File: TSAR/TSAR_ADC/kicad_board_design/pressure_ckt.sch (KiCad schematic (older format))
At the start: 20 parts, among them U10 MCP3424T-E/ST

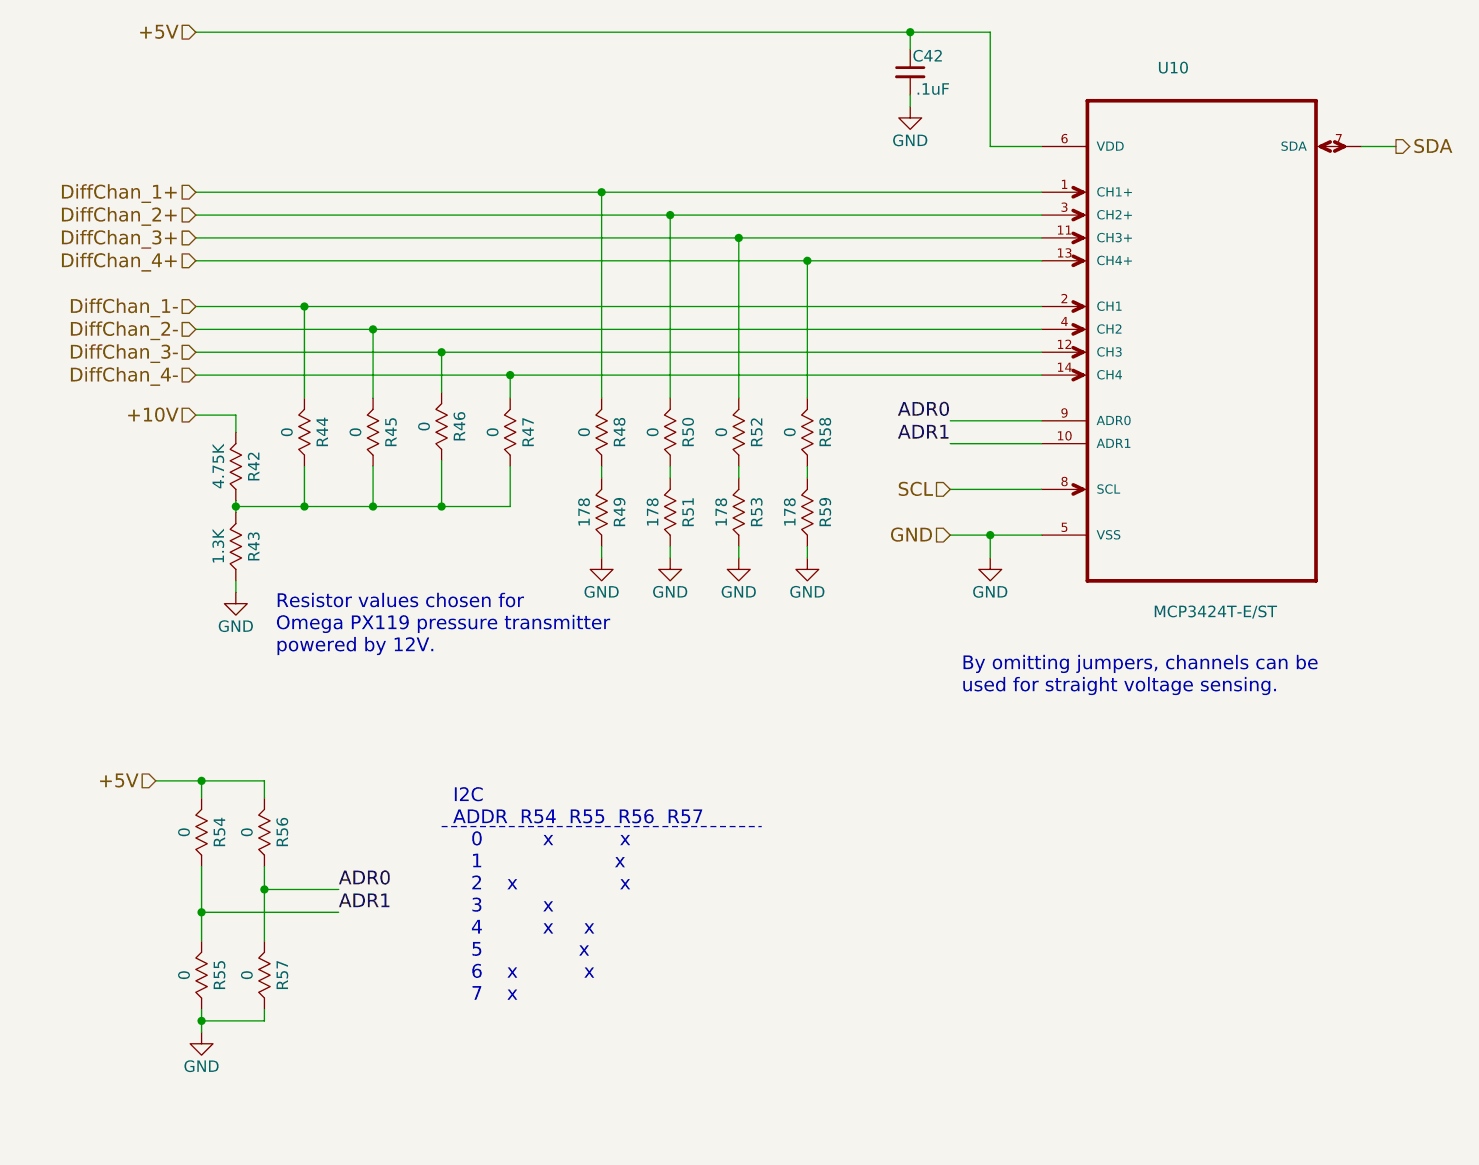
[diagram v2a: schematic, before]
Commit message: Incorporate review comments.  Improve U1 routing, general schematic comments.
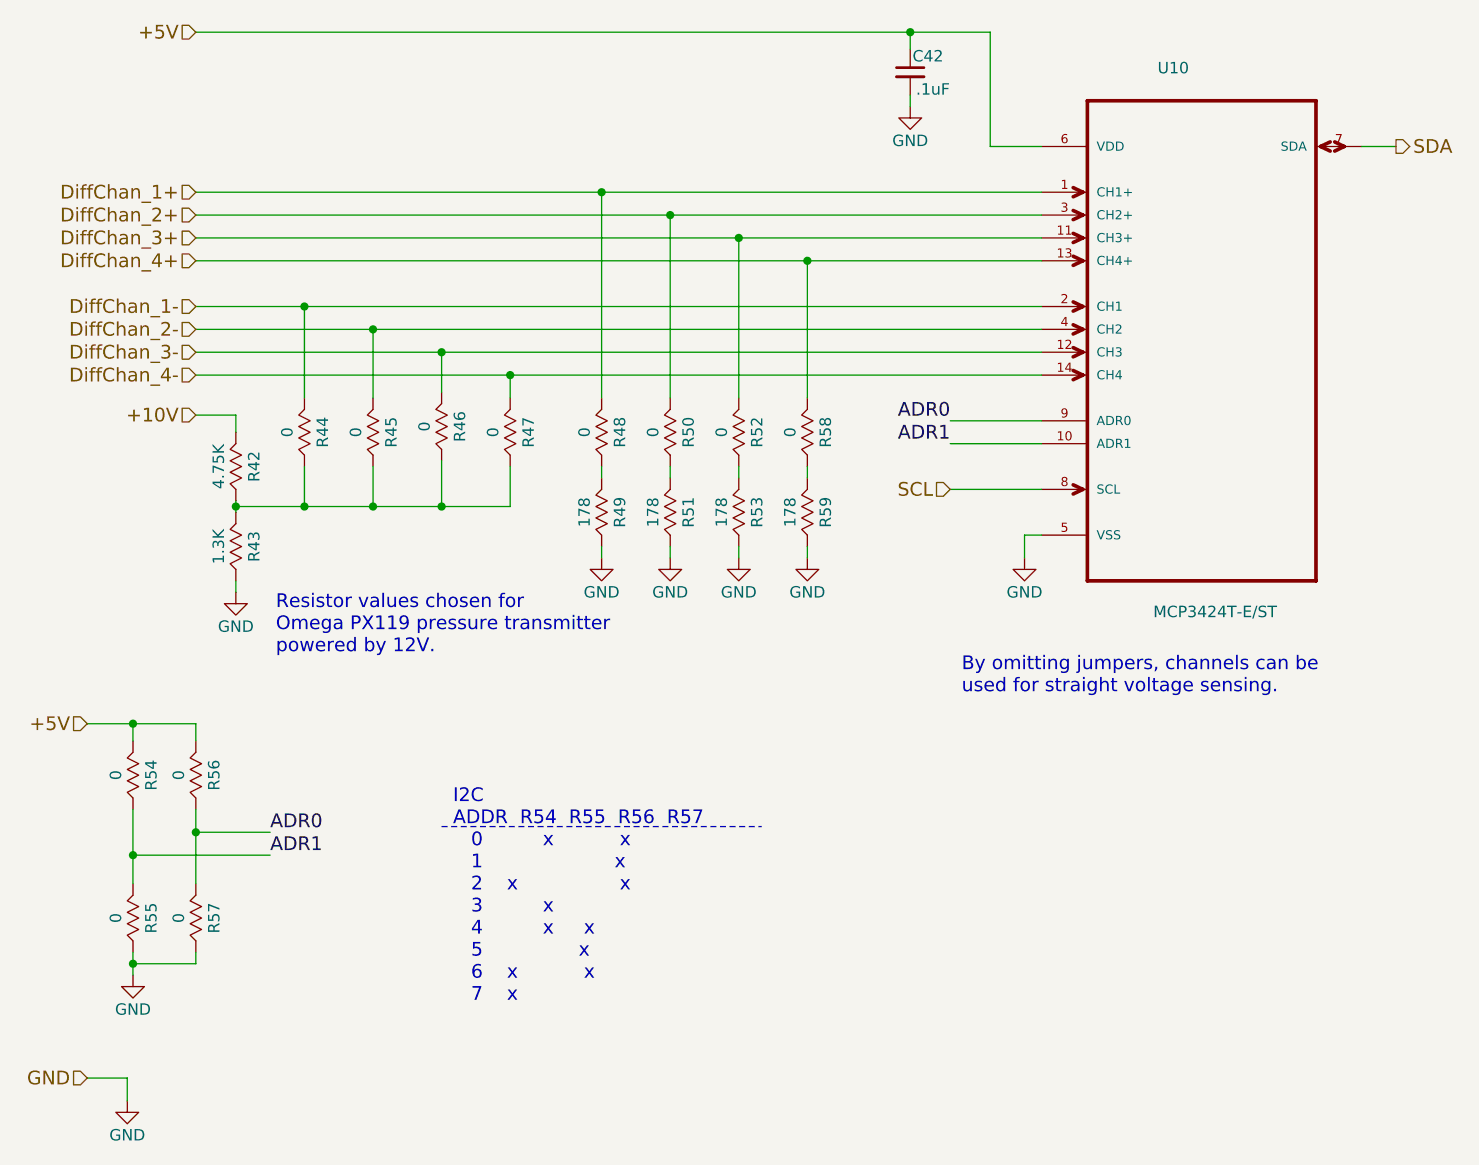
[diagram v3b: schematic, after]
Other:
- moved on the sheet: R54, R55, R56, R57
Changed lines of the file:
@@
 L GND #PWR056
 U 1 1 5B5D17AF
-P 6800 4825
-F 0 "#PWR056" H 6800 4575 50  0001 C CNN
-F 1 "GND" H 6800 4675 50  0000 C CNN
-F 2 "" H 6800 4825 50  0000 C CNN
-F 3 "" H 6800 4825 50  0000 C CNN
-	1    6800 4825
+P 3025 7200
+F 0 "#PWR056" H 3025 6950 50  0001 C CNN
+F 1 "GND" H 3025 7050 50  0000 C CNN
+F 2 "" H 3025 7200 50  0000 C CNN
+F 3 "" H 3025 7200 50  0000 C CNN
+	1    3025 7200
 	1    0    0    -1
 $EndComp
@@
 L GND #PWR062
 U 1 1 5B7B5331
-P 3350 6900
-F 0 "#PWR062" H 3350 6650 50  0001 C CNN
-F 1 "GND" H 3350 6750 50  0000 C CNN
-F 2 "" H 3350 6900 50  0000 C CNN
-F 3 "" H 3350 6900 50  0000 C CNN
-	1    3350 6900
+P 3050 6650
+F 0 "#PWR062" H 3050 6400 50  0001 C CNN
+F 1 "GND" H 3050 6500 50  0000 C CNN
+F 2 "" H 3050 6650 50  0000 C CNN
+F 3 "" H 3050 6650 50  0000 C CNN
+	1    3050 6650
 	1    0    0    -1
 $EndComp
@@
 L R R56
 U 1 1 5B8C8610
-P 3625 6025
-F 0 "R56" V 3705 6025 50  0000 C CNN
-F 1 "0" V 3550 6025 50  0000 C CNN
-F 2 "Resistors_SMD:R_0805_HandSoldering" V 3480 6025 50  0001 C CNN
-F 3 "" H 3550 6025 50  0001 C CNN
-F 4 "ERJ-6GEY0R00V" V 3625 6025 60  0001 C CNN "MPN"
-F 5 "Panasonic" V 3625 6025 60  0001 C CNN "MFN"
-F 6 "Digikey" V 3625 6025 60  0001 C CNN "SPR"
-F 7 "P0.0ACT-ND" V 3625 6025 60  0001 C CNN "SPN"
-F 8 "-" H -2350 -75 50  0001 C CNN "MFR"
-F 9 "-" H -2350 -75 50  0001 C CNN "SPURL"
-	1    3625 6025
+P 3325 5775
+F 0 "R56" V 3405 5775 50  0000 C CNN
+F 1 "0" V 3250 5775 50  0000 C CNN
+F 2 "Resistors_SMD:R_0805_HandSoldering" V 3180 5775 50  0001 C CNN
+F 3 "" H 3250 5775 50  0001 C CNN
+F 4 "ERJ-6GEY0R00V" V 3325 5775 60  0001 C CNN "MPN"
+F 5 "Panasonic" V 3325 5775 60  0001 C CNN "MFN"
+F 6 "Digikey" V 3325 5775 60  0001 C CNN "SPR"
+F 7 "P0.0ACT-ND" V 3325 5775 60  0001 C CNN "SPN"
+F 8 "-" H -2650 -325 50  0001 C CNN "MFR"
+F 9 "-" H -2650 -325 50  0001 C CNN "SPURL"
+	1    3325 5775
 	1    0    0    -1
 $EndComp
@@
 L R R54
 U 1 1 5B8C86F8
-P 3350 6025
-F 0 "R54" V 3430 6025 50  0000 C CNN
-F 1 "0" V 3275 6025 50  0000 C CNN
-F 2 "Resistors_SMD:R_0805_HandSoldering" V 3205 6025 50  0001 C CNN
-F 3 "" H 3275 6025 50  0001 C CNN
-F 4 "ERJ-6GEY0R00V" V 3350 6025 60  0001 C CNN "MPN"
-F 5 "Panasonic" V 3350 6025 60  0001 C CNN "MFN"
-F 6 "Digikey" V 3350 6025 60  0001 C CNN "SPR"
-F 7 "P0.0ACT-ND" V 3350 6025 60  0001 C CNN "SPN"
-F 8 "-" H -2350 -75 50  0001 C CNN "MFR"
-F 9 "-" H -2350 -75 50  0001 C CNN "SPURL"
-	1    3350 6025
+P 3050 5775
+F 0 "R54" V 3130 5775 50  0000 C CNN
+F 1 "0" V 2975 5775 50  0000 C CNN
+F 2 "Resistors_SMD:R_0805_HandSoldering" V 2905 5775 50  0001 C CNN
+F 3 "" H 2975 5775 50  0001 C CNN
+F 4 "ERJ-6GEY0R00V" V 3050 5775 60  0001 C CNN "MPN"
+F 5 "Panasonic" V 3050 5775 60  0001 C CNN "MFN"
+F 6 "Digikey" V 3050 5775 60  0001 C CNN "SPR"
+F 7 "P0.0ACT-ND" V 3050 5775 60  0001 C CNN "SPN"
+F 8 "-" H -2650 -325 50  0001 C CNN "MFR"
+F 9 "-" H -2650 -325 50  0001 C CNN "SPURL"
+	1    3050 5775
 	1    0    0    -1
 $EndComp
@@
 L R R55
 U 1 1 5B8C8758
-P 3350 6650
-F 0 "R55" V 3430 6650 50  0000 C CNN
-F 1 "0" V 3275 6650 50  0000 C CNN
-F 2 "Resistors_SMD:R_0805_HandSoldering" V 3205 6650 50  0001 C CNN
-F 3 "" H 3275 6650 50  0001 C CNN
-F 4 "ERJ-6GEY0R00V" V 3350 6650 60  0001 C CNN "MPN"
-F 5 "Panasonic" V 3350 6650 60  0001 C CNN "MFN"
-F 6 "Digikey" V 3350 6650 60  0001 C CNN "SPR"
-F 7 "P0.0ACT-ND" V 3350 6650 60  0001 C CNN "SPN"
-F 8 "-" H -2350 -75 50  0001 C CNN "MFR"
-F 9 "-" H -2350 -75 50  0001 C CNN "SPURL"
-	1    3350 6650
+P 3050 6400
+F 0 "R55" V 3130 6400 50  0000 C CNN
+F 1 "0" V 2975 6400 50  0000 C CNN
+F 2 "Resistors_SMD:R_0805_HandSoldering" V 2905 6400 50  0001 C CNN
+F 3 "" H 2975 6400 50  0001 C CNN
+F 4 "ERJ-6GEY0R00V" V 3050 6400 60  0001 C CNN "MPN"
+F 5 "Panasonic" V 3050 6400 60  0001 C CNN "MFN"
+F 6 "Digikey" V 3050 6400 60  0001 C CNN "SPR"
+F 7 "P0.0ACT-ND" V 3050 6400 60  0001 C CNN "SPN"
+F 8 "-" H -2650 -325 50  0001 C CNN "MFR"
+F 9 "-" H -2650 -325 50  0001 C CNN "SPURL"
+	1    3050 6400
 	1    0    0    -1
 $EndComp
@@
 L R R57
 U 1 1 5B8C87E9
-P 3625 6650
-F 0 "R57" V 3705 6650 50  0000 C CNN
-F 1 "0" V 3550 6650 50  0000 C CNN
-F 2 "Resistors_SMD:R_0805_HandSoldering" V 3480 6650 50  0001 C CNN
-F 3 "" H 3550 6650 50  0001 C CNN
-F 4 "ERJ-6GEY0R00V" V 3625 6650 60  0001 C CNN "MPN"
-F 5 "Panasonic" V 3625 6650 60  0001 C CNN "MFN"
-F 6 "Digikey" V 3625 6650 60  0001 C CNN "SPR"
-F 7 "P0.0ACT-ND" V 3625 6650 60  0001 C CNN "SPN"
-F 8 "-" H -2350 -75 50  0001 C CNN "MFR"
-F 9 "-" H -2350 -75 50  0001 C CNN "SPURL"
-	1    3625 6650
+P 3325 6400
+F 0 "R57" V 3405 6400 50  0000 C CNN
+F 1 "0" V 3250 6400 50  0000 C CNN
+F 2 "Resistors_SMD:R_0805_HandSoldering" V 3180 6400 50  0001 C CNN
+F 3 "" H 3250 6400 50  0001 C CNN
+F 4 "ERJ-6GEY0R00V" V 3325 6400 60  0001 C CNN "MPN"
+F 5 "Panasonic" V 3325 6400 60  0001 C CNN "MFN"
+F 6 "Digikey" V 3325 6400 60  0001 C CNN "SPR"
+F 7 "P0.0ACT-ND" V 3325 6400 60  0001 C CNN "SPN"
+F 8 "-" H -2650 -325 50  0001 C CNN "MFR"
+F 9 "-" H -2650 -325 50  0001 C CNN "SPURL"
+	1    3325 6400
 	1    0    0    -1
 $EndComp
@@
 Text HLabel 3325 4025 0    60   Input ~ 0
 DiffChan_4-
-Text HLabel 6625 4725 0    60   Input ~ 0
+Text HLabel 2850 7100 0    60   Input ~ 0
 GND
 Text HLabel 3325 4200 0    60   Input ~ 0
 +10V
-Text Label 3950 6275 0    60   ~ 0
+Text Label 3650 6025 0    60   ~ 0
 ADR0
-Text Label 3950 6375 0    60   ~ 0
+Text Label 3650 6125 0    60   ~ 0
 ADR1
-Text HLabel 3150 5800 0    60   Input ~ 0
+Text HLabel 2850 5550 0    60   Input ~ 0
 +5V
 Text Label 6625 4225 2    60   ~ 0
@@
 ADR1
 Wire Wire Line
-	6625 4725 6800 4725
-Wire Wire Line
-	6800 4725 7025 4725
-Wire Wire Line
-	6800 4725 6800 4825
-Wire Wire Line
 	7025 4225 6625 4225
 Wire Wire Line
@@
 	8425 3025 8575 3025
 Wire Wire Line
-	3325 3225 5100 3225
-Wire Wire Line
-	5100 3225 7025 3225
-Wire Wire Line
-	3325 3325 5400 3325
-Wire Wire Line
-	5400 3325 7025 3325
-Wire Wire Line
-	3325 3425 5700 3425
-Wire Wire Line
-	5700 3425 7025 3425
-Wire Wire Line
-	3325 3525 6000 3525
-Wire Wire Line
-	6000 3525 7025 3525
-Wire Wire Line
-	3325 3725 3800 3725
-Wire Wire Line
-	3800 3725 7025 3725
-Wire Wire Line
-	3325 3825 4100 3825
-Wire Wire Line
-	4100 3825 7025 3825
-Wire Wire Line
-	3325 3925 4400 3925
-Wire Wire Line
-	4400 3925 7025 3925
-Wire Wire Line
-	3325 4025 4700 4025
-Wire Wire Line
-	4700 4025 7025 4025
+	3325 3225 7025 3225
+Wire Wire Line
+	3325 3325 7025 3325
+Wire Wire Line
+	3325 3425 7025 3425
+Wire Wire Line
+	3325 3525 7025 3525
+Wire Wire Line
+	3325 3725 7025 3725
+Wire Wire Line
+	3325 3825 7025 3825
+Wire Wire Line
+	3325 3925 7025 3925
+Wire Wire Line
+	3325 4025 7025 4025
 Wire Wire Line
 	5100 4825 5100 4775
@@
 	3800 4425 3800 4600
 Wire Wire Line
-	4100 4425 4100 4600
+	4100 4600 4100 4425
 Wire Wire Line
 	4700 4600 4700 4425
@@
 	3500 4975 3500 4925
 Wire Wire Line
-	3500 4575 3500 4600
-Wire Wire Line
-	3500 4600 3500 4625
+	3500 4575 3500 4625
 Wire Wire Line
 	3325 4200 3500 4200
@@
 	3500 4200 3500 4275
 Wire Wire Line
-	3500 4600 3800 4600
-Wire Wire Line
-	3800 4600 4100 4600
-Wire Wire Line
-	4100 4600 4400 4600
-Wire Wire Line
-	4400 4600 4700 4600
-Wire Wire Line
-	3150 5800 3350 5800
-Wire Wire Line
-	3350 5800 3625 5800
-Wire Wire Line
-	3350 5800 3350 5875
-Wire Wire Line
-	3625 5800 3625 5875
-Wire Wire Line
-	3350 6175 3350 6375
-Wire Wire Line
-	3350 6375 3350 6500
-Wire Wire Line
-	3625 6175 3625 6275
-Wire Wire Line
-	3625 6275 3625 6500
+	3500 4600 4700 4600
+Wire Wire Line
+	2850 5550 3325 5550
+Wire Wire Line
+	3050 5550 3050 5625
+Wire Wire Line
+	3325 5550 3325 5625
+Wire Wire Line
+	3050 5925 3050 6250
+Wire Wire Line
+	3325 5925 3325 6250
 Wire Wire Line
 	6450 2850 6450 2800
@@
 	7025 3025 6800 3025
 Wire Wire Line
-	6800 3025 6800 2525
-Wire Wire Line
-	6800 2525 6450 2525
-Wire Wire Line
-	6450 2525 3325 2525
+	6800 2525 6800 3025
+Wire Wire Line
+	3325 2525 6800 2525
 Wire Wire Line
 	6450 2525 6450 2600
-Connection ~ 6800 4725
 Connection ~ 5100 3225
 Connection ~ 5400 3325
@@
 Connection ~ 4100 4600
 Connection ~ 3800 4600
-Connection ~ 3350 5800
-Connection ~ 3350 6375
-Connection ~ 3625 6275
+Connection ~ 3050 5550
+Connection ~ 3050 6125
+Connection ~ 3325 6025
 Connection ~ 6450 2525
 Wire Wire Line
 	4400 4400 4400 4600
 Wire Wire Line
-	3625 6800 3625 6850
-Wire Wire Line
-	3625 6850 3350 6850
-Wire Wire Line
-	3350 6800 3350 6850
-Wire Wire Line
-	3350 6850 3350 6900
-Connection ~ 3350 6850
+	3325 6550 3325 6600
+Wire Wire Line
+	3325 6600 3050 6600
+Wire Wire Line
+	3050 6550 3050 6650
+Connection ~ 3050 6600
 Text Notes 3675 5250 0    60   ~ 0
 Resistor values chosen for \nOmega PX119 pressure transmitter\npowered by 12V.
@@
 	4400 6000 5800 6000
 Wire Wire Line
-	3625 6275 3950 6275
-Wire Wire Line
-	3350 6375 3950 6375
+	3325 6025 3650 6025
+Wire Wire Line
+	3050 6125 3650 6125
+Wire Wire Line
+	3025 7100 3025 7200
+Wire Wire Line
+	2850 7100 3025 7100
+$Comp
+L GND #PWR?
+U 1 1 5BF59367
+P 6950 4825
+F 0 "#PWR?" H 6950 4575 50  0001 C CNN
+F 1 "GND" H 6950 4675 50  0000 C CNN
+F 2 "" H 6950 4825 50  0000 C CNN
+F 3 "" H 6950 4825 50  0000 C CNN
+	1    6950 4825
+	1    0    0    -1
+$EndComp
+Wire Wire Line
+	7025 4725 6950 4725
+Wire Wire Line
+	6950 4725 6950 4825
 $EndSCHEMATC
